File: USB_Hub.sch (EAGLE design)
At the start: 56 parts, among them CON1 USB-ZX62, CON2 USB-5075AR-04-WH, CON3 USB-5075AR-04-WH, CON4 USB-5075AR-04-WH, CON5 USB-5075AR-04-WH, IC1 UPD720115, IC2 AP22652, J1 BUS/SELF, J2 VBUS, SW1 RESET, X1 24MHz

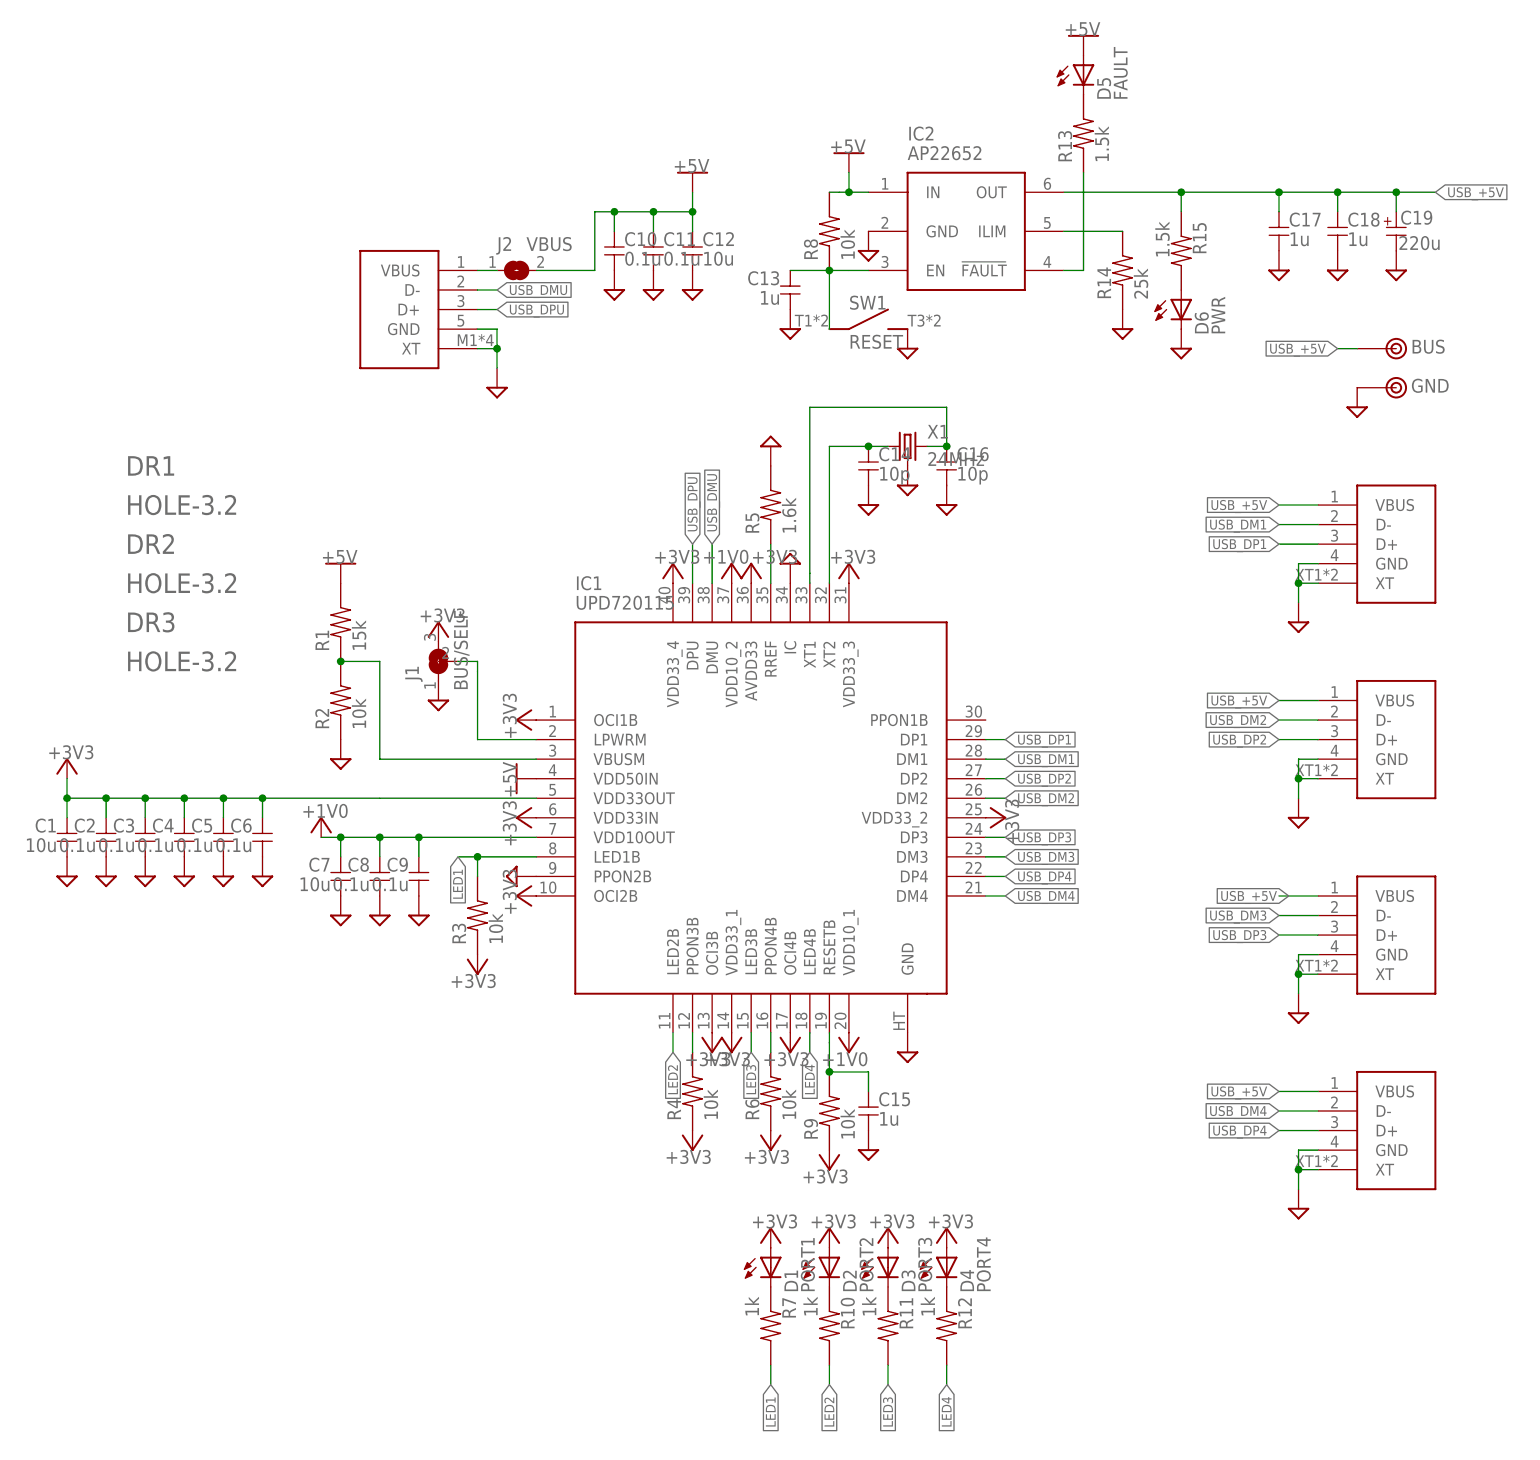
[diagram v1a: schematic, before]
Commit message: Type-Cに変更
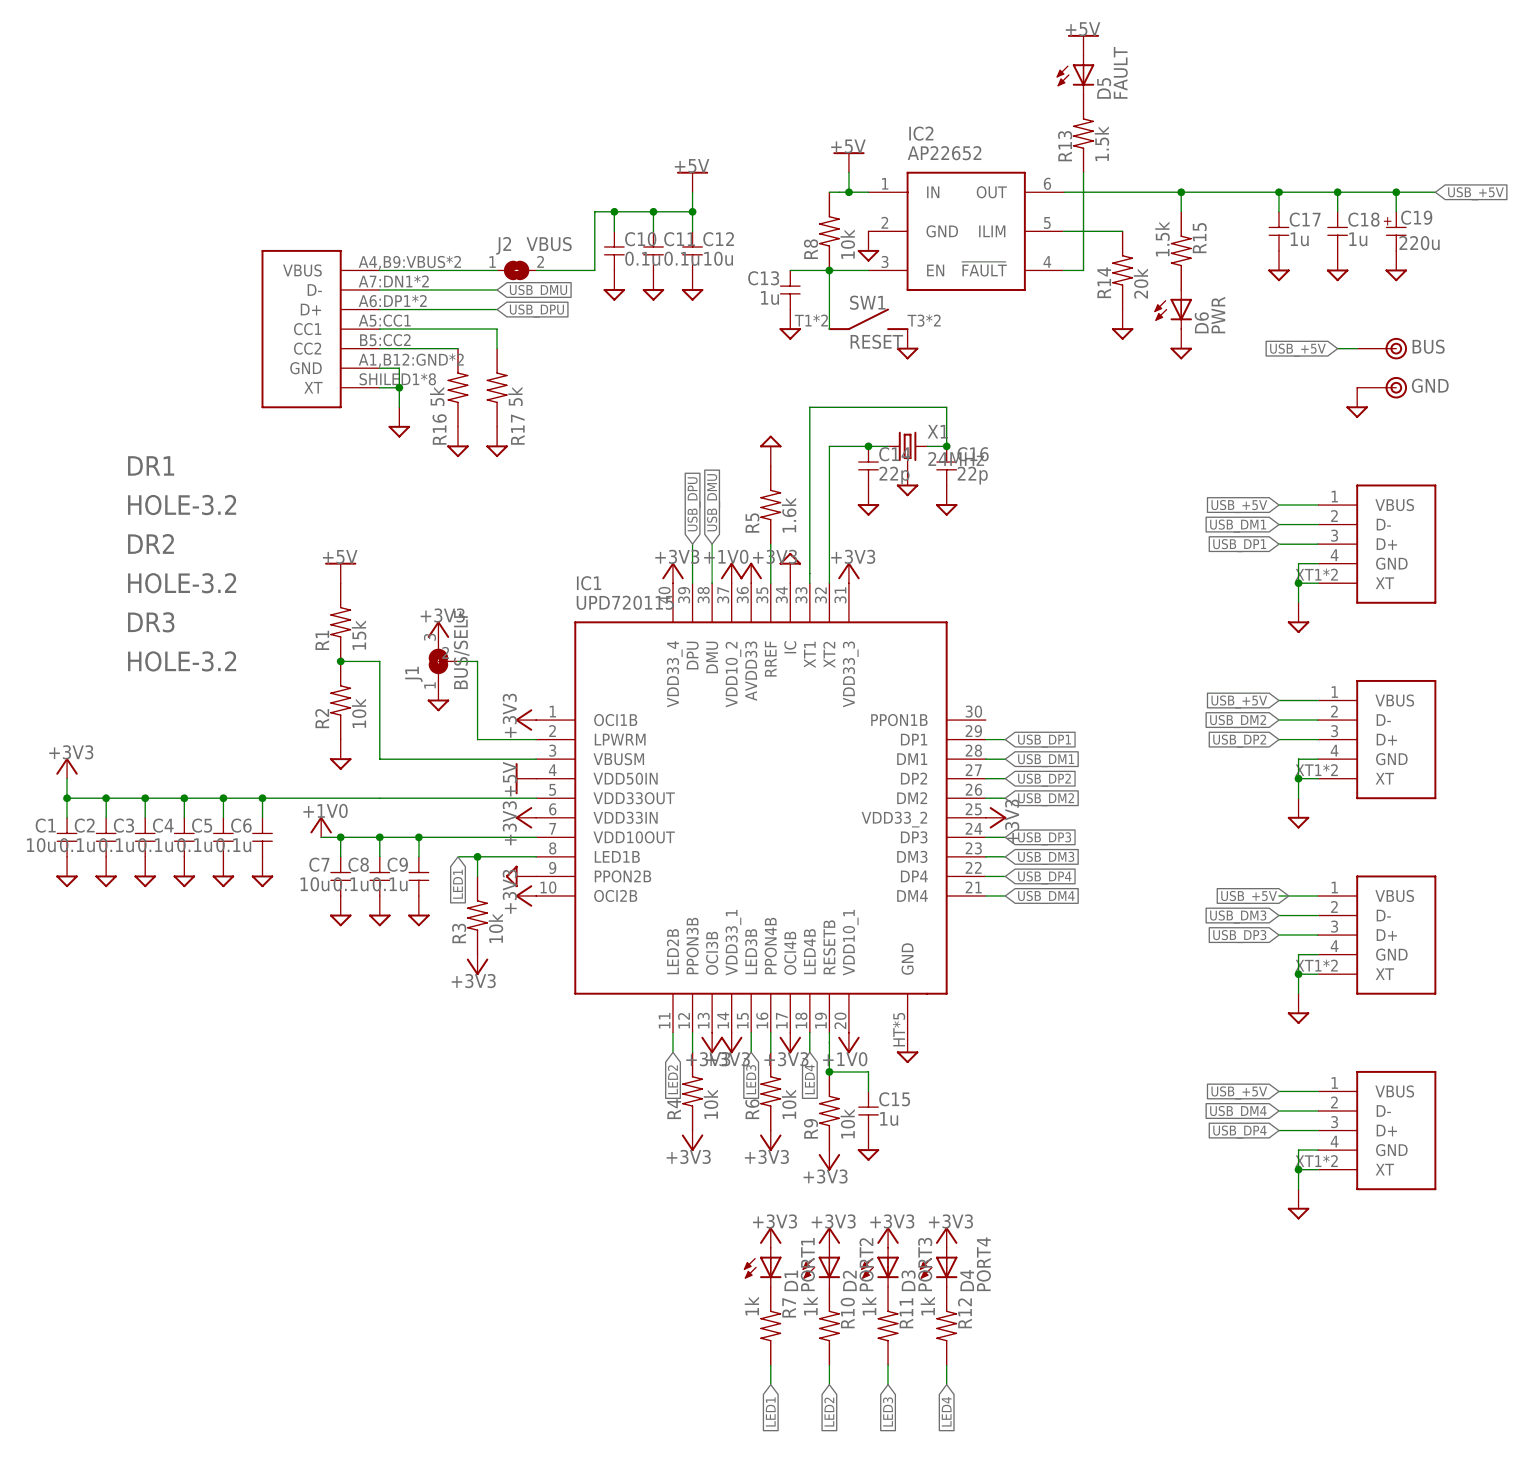
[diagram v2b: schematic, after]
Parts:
- added R16, R17: 5k, my_rcl:R-1608
- C14, C16: value 10p -> 22p
- CON1: value USB-ZX62 -> USB-C; device my_connector:USB-ZX62 -> my_connector:USB-C
- J2: device my_rcl:SJ-2012 -> my_rcl:SJ-1608
- R14: value 25k -> 20k
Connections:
- new net N$18: CON1.CC2, R16.2
- new net N$19: CON1.CC1, R17.2
- net GND: now also R16.1, R17.1
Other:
- moved on the sheet: IC1
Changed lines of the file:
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@@
 <layer number="132" name="bAdjust" color="7" fill="1" visible="yes" active="yes"/>
 <layer number="133" name="bottom_silk" color="7" fill="1" visible="no" active="no"/>
+<layer number="134" name="silk_top" color="7" fill="1" visible="no" active="no"/>
+<layer number="135" name="silk_bottom" color="7" fill="1" visible="no" active="no"/>
+<layer number="136" name="silktop" color="7" fill="1" visible="no" active="no"/>
+<layer number="137" name="silkbottom" color="7" fill="1" visible="no" active="no"/>
+<layer number="138" name="EEE" color="7" fill="1" visible="no" active="no"/>
+<layer number="139" name="_tKeepout" color="7" fill="1" visible="no" active="no"/>
+<layer number="141" name="ASSEMBLY_TOP" color="7" fill="1" visible="no" active="no"/>
+<layer number="143" name="PLACE_BOUND_TOP" color="7" fill="1" visible="no" active="no"/>
 <layer number="144" name="Drill_legend" color="7" fill="1" visible="no" active="no"/>
+<layer number="145" name="DrillLegend_01-16" color="7" fill="1" visible="no" active="no"/>
+<layer number="146" name="DrillLegend_01-20" color="7" fill="1" visible="no" active="no"/>
+<layer number="147" name="PIN_NUMBER" color="7" fill="1" visible="no" active="no"/>
 <layer number="150" name="Notes" color="7" fill="1" visible="no" active="no"/>
 <layer number="151" name="HeatSink" color="7" fill="1" visible="yes" active="yes"/>
@@
 <class number="0" name="default" width="0" drill="0">
 </class>
+<class number="1" name="Power" width="0.254" drill="0">
+</class>
 </classes>
 <parts>
-<part name="CON1" library="my_connector" deviceset="USB" device="-ZX62"/>
 <part name="SUPPLY1" library="my_supply" deviceset="GND" device=""/>
 <part name="IC1" library="my_ic" deviceset="UPD720115" device=""/>
@@
 <part name="SUPPLY4" library="my_supply" deviceset="GND" device=""/>
 <part name="X1" library="my_rcl" deviceset="CRYSTAL2" device="" value="24MHz"/>
-<part name="C14" library="my_rcl" deviceset="C" device="-1608" value="10p"/>
-<part name="C16" library="my_rcl" deviceset="C" device="-1608" value="10p"/>
+<part name="C14" library="my_rcl" deviceset="C" device="-1608" value="22p"/>
+<part name="C16" library="my_rcl" deviceset="C" device="-1608" value="22p"/>
 <part name="SUPPLY5" library="my_supply" deviceset="GND" device=""/>
 <part name="SUPPLY6" library="my_supply" deviceset="GND" device=""/>
@@
 <part name="SUPPLY17" library="my_supply" deviceset="GND" device=""/>
 <part name="+3V15" library="my_supply" deviceset="+3V3" device=""/>
-<part name="J2" library="my_rcl" deviceset="SJ" device="-2012" value="VBUS"/>
+<part name="J2" library="my_rcl" deviceset="SJ" device="-1608" value="VBUS"/>
 <part name="R7" library="my_rcl" deviceset="R" device="-1608" value="1k"/>
 <part name="R10" library="my_rcl" deviceset="R" device="-1608" value="1k"/>
@@
 <part name="P6" library="my_supply" deviceset="+5V" device=""/>
 <part name="SUPPLY25" library="my_supply" deviceset="GND" device=""/>
-<part name="R14" library="my_rcl" deviceset="R" device="-1608" value="25k"/>
+<part name="R14" library="my_rcl" deviceset="R" device="-1608" value="20k"/>
 <part name="SUPPLY26" library="my_supply" deviceset="GND" device=""/>
 <part name="C19" library="my_rcl" deviceset="CPOL" device="E2.5-6.5" value="220u"/>
@@
 <part name="C18" library="my_rcl" deviceset="C" device="-1608" value="1u"/>
 <part name="SUPPLY36" library="my_supply" deviceset="GND" device=""/>
+<part name="CON1" library="my_connector" deviceset="USB-C" device=""/>
+<part name="R16" library="my_rcl" deviceset="R" device="-1608" value="5k"/>
+<part name="R17" library="my_rcl" deviceset="R" device="-1608" value="5k"/>
+<part name="SUPPLY37" library="my_supply" deviceset="GND" device=""/>
+<part name="SUPPLY38" library="my_supply" deviceset="GND" device=""/>
 </parts>
 <sheets>
@@
 </plain>
 <instances>
-<instance part="CON1" gate="G$1" x="-20.32" y="127" smashed="yes">
-<attribute name="NAME" x="-22.86" y="133.35" size="1.778" layer="104"/>
-<attribute name="VALUE" x="-24.13" y="114.3" size="1.778" layer="104"/>
-</instance>
-<instance part="SUPPLY1" gate="GND" x="-5.08" y="114.3" smashed="yes"/>
+<instance part="SUPPLY1" gate="GND" x="-17.78" y="109.22" smashed="yes"/>
 <instance part="IC1" gate="G$1" x="27.94" y="60.96" smashed="yes">
 <attribute name="NAME" x="5.08" y="88.9" size="1.778" layer="95" align="center-left"/>
@@
 </instance>
 <instance part="SUPPLY36" gate="GND" x="104.14" y="129.54" smashed="yes"/>
+<instance part="CON1" gate="G$1" x="-33.02" y="121.92" smashed="yes">
+<attribute name="NAME" x="-35.56" y="133.35" size="1.778" layer="104"/>
+<attribute name="VALUE" x="-35.56" y="109.22" size="1.778" layer="104"/>
+</instance>
+<instance part="R16" gate="G$1" x="-10.16" y="114.3" smashed="yes" rot="R90">
+<attribute name="NAME" x="-11.6586" y="106.68" size="1.778" layer="95" rot="R90"/>
+<attribute name="VALUE" x="-11.938" y="111.76" size="1.778" layer="96" rot="R90"/>
+</instance>
+<instance part="R17" gate="G$1" x="-5.08" y="114.3" smashed="yes" rot="R90">
+<attribute name="NAME" x="-1.4986" y="106.68" size="1.778" layer="95" rot="R90"/>
+<attribute name="VALUE" x="-1.778" y="111.76" size="1.778" layer="96" rot="R90"/>
+</instance>
+<instance part="SUPPLY37" gate="GND" x="-10.16" y="106.68" smashed="yes"/>
+<instance part="SUPPLY38" gate="GND" x="-5.08" y="106.68" smashed="yes"/>
 </instances>
 <busses>
@@
 <net name="GND" class="0">
 <segment>
+<pinref part="SUPPLY1" gate="GND" pin="GND"/>
+<wire x1="-20.32" y1="116.84" x2="-17.78" y2="116.84" width="0.1524" layer="91"/>
+<wire x1="-17.78" y1="116.84" x2="-17.78" y2="114.3" width="0.1524" layer="91"/>
+<wire x1="-17.78" y1="114.3" x2="-17.78" y2="111.76" width="0.1524" layer="91"/>
+<wire x1="-20.32" y1="114.3" x2="-17.78" y2="114.3" width="0.1524" layer="91"/>
+<junction x="-17.78" y="114.3"/>
 <pinref part="CON1" gate="G$1" pin="GND"/>
-<pinref part="SUPPLY1" gate="GND" pin="GND"/>
-<wire x1="-7.62" y1="121.92" x2="-5.08" y2="121.92" width="0.1524" layer="91"/>
-<wire x1="-5.08" y1="121.92" x2="-5.08" y2="119.38" width="0.1524" layer="91"/>
 <pinref part="CON1" gate="G$1" pin="XT"/>
-<wire x1="-5.08" y1="119.38" x2="-5.08" y2="116.84" width="0.1524" layer="91"/>
-<wire x1="-7.62" y1="119.38" x2="-5.08" y2="119.38" width="0.1524" layer="91"/>
-<junction x="-5.08" y="119.38"/>
 </segment>
 <segment>
@@
 <pinref part="C18" gate="G$1" pin="2"/>
 <pinref part="SUPPLY36" gate="GND" pin="GND"/>
+</segment>
+<segment>
+<pinref part="R16" gate="G$1" pin="1"/>
+<pinref part="SUPPLY37" gate="GND" pin="GND"/>
+</segment>
+<segment>
+<pinref part="R17" gate="G$1" pin="1"/>
+<pinref part="SUPPLY38" gate="GND" pin="GND"/>
 </segment>
 </net>
@@
 </segment>
 </net>
-<net name="+3V3" class="0">
+<net name="+3V3" class="1">
 <segment>
 <pinref part="IC1" gate="G$1" pin="VDD33_3"/>
@@
 </segment>
 </net>
-<net name="+1V0" class="0">
+<net name="+1V0" class="1">
 <segment>
 <pinref part="IC1" gate="G$1" pin="VDD10_1"/>
@@
 </segment>
 <segment>
+<wire x1="-20.32" y1="124.46" x2="-5.08" y2="124.46" width="0.1524" layer="91"/>
+<label x="-5.08" y="124.46" size="1.27" layer="95" xref="yes"/>
 <pinref part="CON1" gate="G$1" pin="D+"/>
-<wire x1="-7.62" y1="124.46" x2="-5.08" y2="124.46" width="0.1524" layer="91"/>
-<label x="-5.08" y="124.46" size="1.27" layer="95" xref="yes"/>
 </segment>
 </net>
@@
 </segment>
 <segment>
+<wire x1="-20.32" y1="127" x2="-5.08" y2="127" width="0.1524" layer="91"/>
+<label x="-5.08" y="127" size="1.27" layer="95" xref="yes"/>
 <pinref part="CON1" gate="G$1" pin="D-"/>
-<wire x1="-7.62" y1="127" x2="-5.08" y2="127" width="0.1524" layer="91"/>
-<label x="-5.08" y="127" size="1.27" layer="95" xref="yes"/>
 </segment>
 </net>
@@
 <net name="N$1" class="0">
 <segment>
+<pinref part="J2" gate="G$1" pin="1"/>
+<wire x1="-20.32" y1="129.54" x2="-5.08" y2="129.54" width="0.1524" layer="91"/>
 <pinref part="CON1" gate="G$1" pin="VBUS"/>
-<pinref part="J2" gate="G$1" pin="1"/>
-<wire x1="-7.62" y1="129.54" x2="-5.08" y2="129.54" width="0.1524" layer="91"/>
 </segment>
 </net>
@@
 </segment>
 </net>
+<net name="N$18" class="0">
+<segment>
+<pinref part="CON1" gate="G$1" pin="CC2"/>
+<pinref part="R16" gate="G$1" pin="2"/>
+<wire x1="-20.32" y1="119.38" x2="-10.16" y2="119.38" width="0.1524" layer="91"/>
+</segment>
+</net>
+<net name="N$19" class="0">
+<segment>
+<pinref part="CON1" gate="G$1" pin="CC1"/>
+<pinref part="R17" gate="G$1" pin="2"/>
+<wire x1="-20.32" y1="121.92" x2="-5.08" y2="121.92" width="0.1524" layer="91"/>
+<wire x1="-5.08" y1="121.92" x2="-5.08" y2="119.38" width="0.1524" layer="91"/>
+</segment>
+</net>
